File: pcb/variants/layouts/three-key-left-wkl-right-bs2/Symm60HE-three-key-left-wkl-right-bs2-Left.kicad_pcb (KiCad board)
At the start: 2 copper layers, 145.9 x 104.7 mm, 173 parts

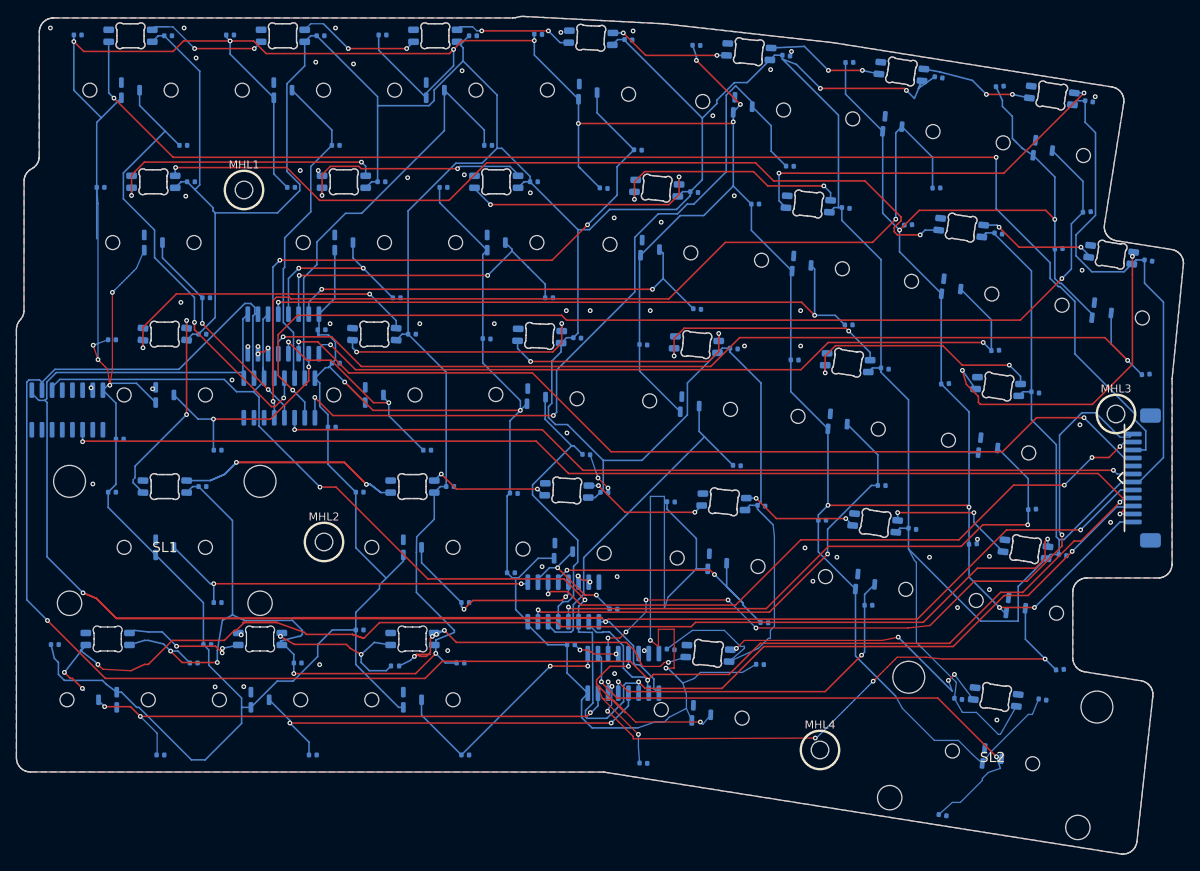
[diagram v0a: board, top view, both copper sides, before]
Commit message: Move every LED into the switch's south RGB pocket
The reverse-mount SK6812MINI-E sat 7.60 mm north of each key, shining into
the Gateron KS-20's opaque cover rather than its window. All 65 LEDs now sit
5.35 mm south of their key, in the pocket the cover is moulded for, so the
board lights like a Wooting 60HE+ backlight instead of a pass-through for a
transparent cap. Switches install with their RGB pocket toward the user; the
plate cutout and the alignment pins are symmetric, so nothing else changes.

Both halves were re-routed around the new apertures and are fully connected
with no DRC errors: 247 vias on the left (was 251) and 418 on the right (was
393). A handful of GND pads the apertures fence off on both layers reach the
plane through a via inside the pad, so the order checklist now asks for tented
vias. The pours' copies of the apertures moved with the LEDs -- they had been
left behind at the old positions, cutting some 800 mm2 of ground per layer for
openings that were no longer there.

The fixed-layout derivatives needed more than a copy of that work. Each one
restores its close-pair switches' alignment drills to the horizontal axis, and
the masters' new routing ran where those drills land, so the finishing pass
grew a repair loop: give a finding room, route it again, and keep the result
only if nothing got worse -- no new opens, and never a short. A net the router
cannot put back keeps the copper it had. Where a gap is short by microns the
trace is bent clear rather than ripped, because on a board this full a ripped
trace comes back exactly where it was. An LED only returns to its fixed-layout
row when that space is free, and the stabilisers keep the master's angle now
that they no longer have a northern aperture to face. All sixteen boards report
zero DRC and connectivity errors, and the audit checks the pocket window rather
than a nominal offset.

The panel gained the same care: a break row would have drilled through a trace
running along the right half'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
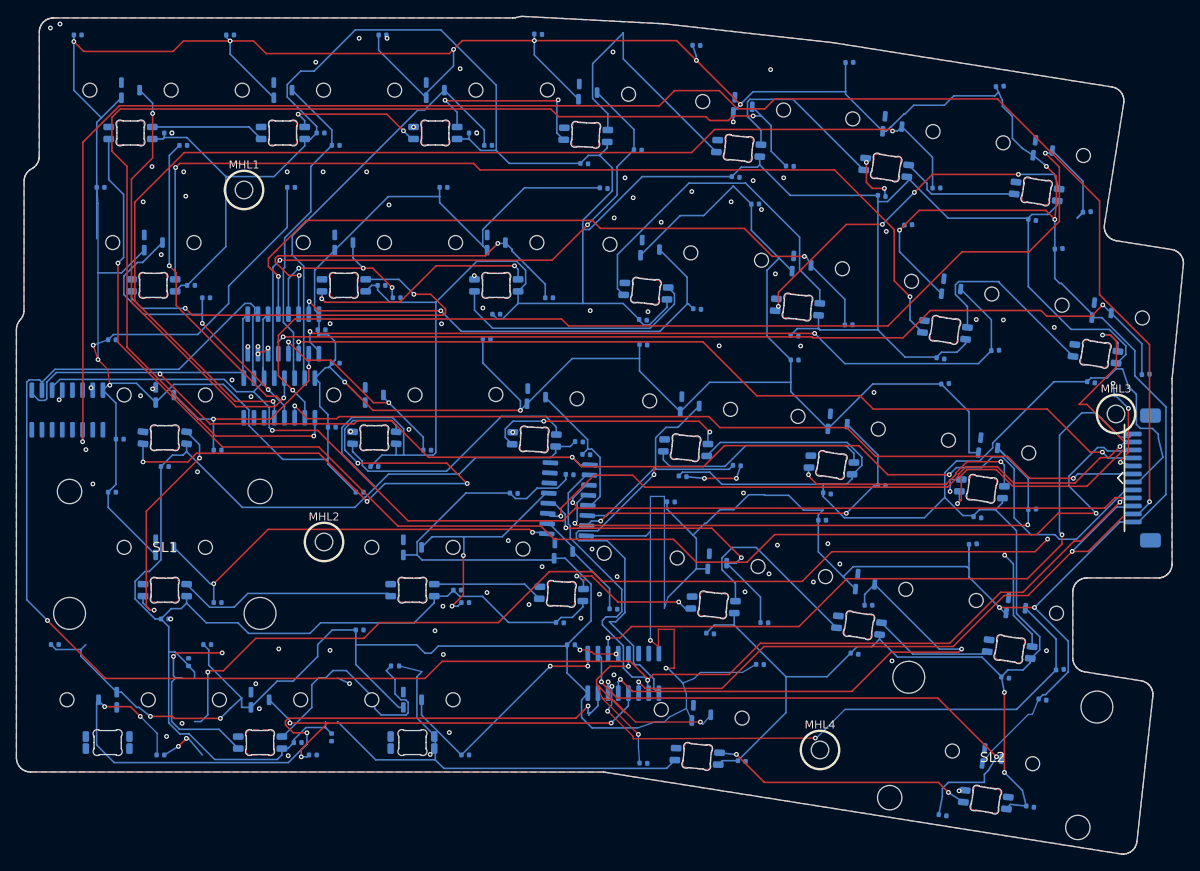
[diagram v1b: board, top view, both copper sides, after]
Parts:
- moved CRGBL29 18.6 mm to (38.9, 90.4), turned to -90 degrees
- moved CRGBL17 17.2 mm to (82.8, 57.8)
- moved CRGBL19 17.2 mm to (44.3, 56.6)
- moved CRGBL20 17.2 mm to (18.1, 56.6)
- moved CRGBL21 17.2 mm to (18.1, 75.6)
- moved CRGBL8 17.2 mm to (96.8, 40.2)
- moved CRGBL13 17.2 mm to (115.1, 43.1)
- moved CRGBL10 17.2 mm to (59.5, 37.5)
- moved CRGBL25 17.2 mm to (104.3, 80.0)
- moved CRGBL9 17.2 mm to (77.9, 38.2)
- moved CRGBL24 17.2 mm to (86.3, 77.4)
- moved CRGBL15 17.2 mm to (119.7, 62.9)
- moved CRGBL16 17.2 mm to (100.9, 59.9)
- moved CRGBL23 17.2 mm to (67.5, 76.1)
- moved CRGBL26 16.9 mm to (123.1, 83.0)
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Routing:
- net +3V3A: track 942.3 -> 1059.3 mm, vias 22 -> 21
- net MUX_A2: track 321.2 -> 224.2 mm, vias 3 -> 4
- net ADC_L5: track 138.4 -> 218.5 mm
- net HE_L05: track 98.5 -> 152.0 mm
- net MUX_A0: track 192.4 -> 244.1 mm
- net HE_L01: track 57.7 -> 94.6 mm, vias 2 -> 3
- net RGB_L_19: track 39.2 -> 74.3 mm, vias 2 -> 4
- net GND: track 16.4 -> 47.2 mm, vias 68 -> 104
- net HE_L06: track 118.1 -> 146.2 mm
- net VBUS: track 777.2 -> 801.5 mm, vias 6 -> 2
- net RGB_L_21: track 51.4 -> 27.6 mm, vias 2 -> 0
- net MUX_A1: track 238.3 -> 260.8 mm
- net HE_L27: track 72.0 -> 94.0 mm, vias 3 -> 4
- net HE_L25: track 43.8 -> 64.7 mm
- net RGB_L_04: track 15.4 -> 34.2 mm, vias 2 -> 0
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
